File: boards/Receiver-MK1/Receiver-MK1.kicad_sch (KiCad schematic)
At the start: 0 parts

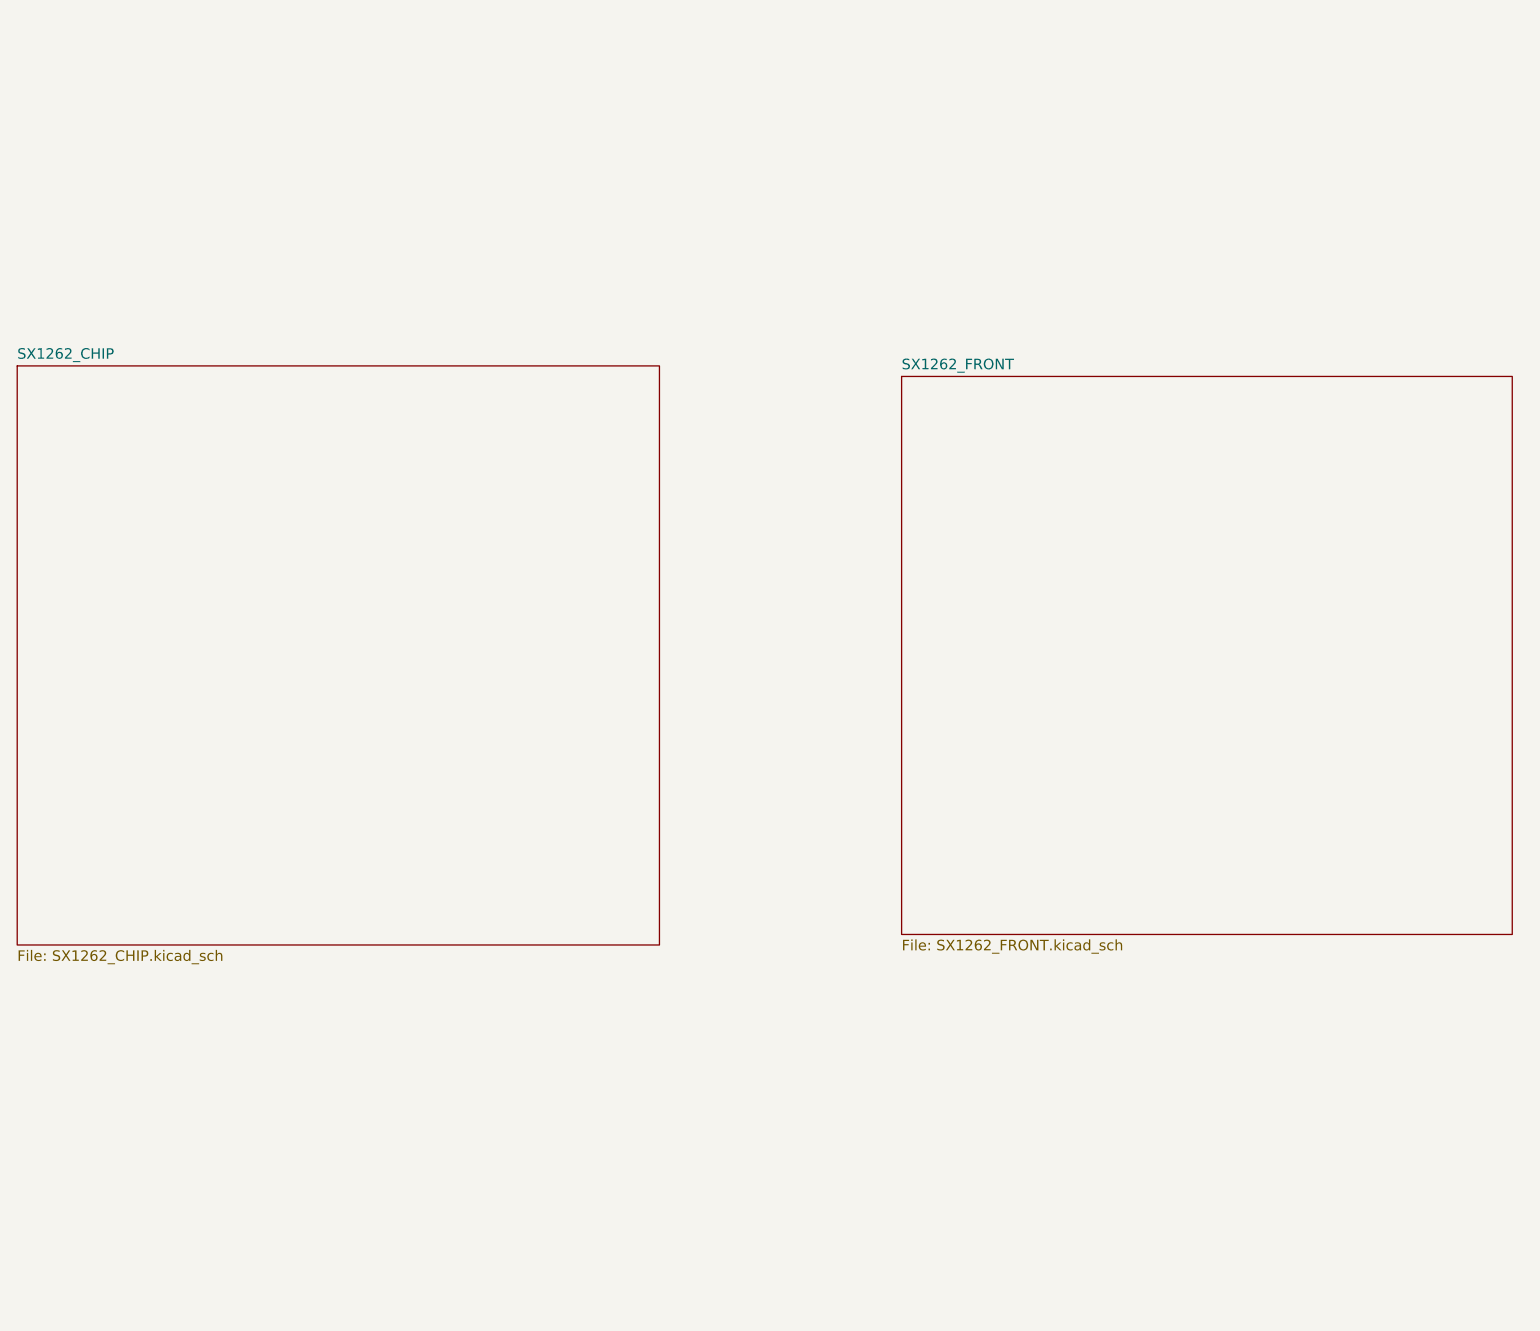
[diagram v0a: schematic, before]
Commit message: Added Transceiver
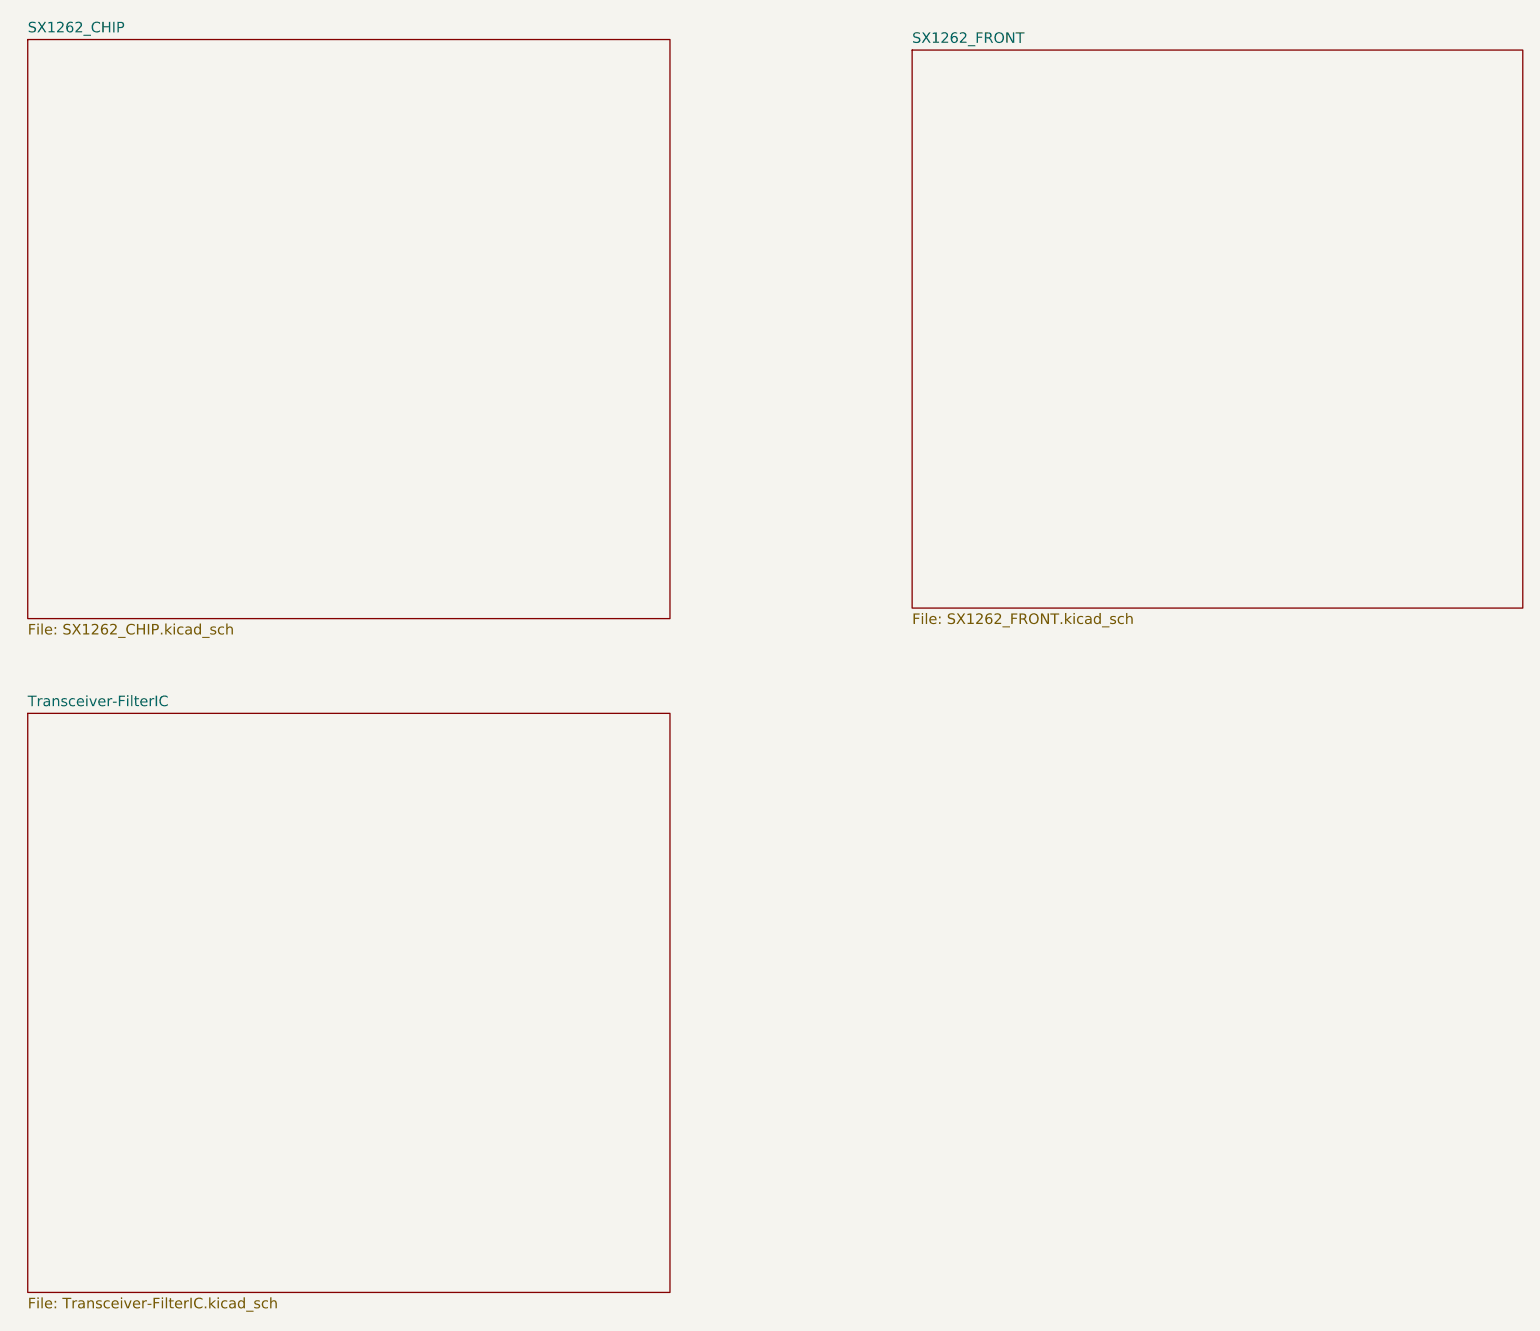
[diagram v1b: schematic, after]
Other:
- added sheet Transceiver-FilterIC (Transceiver-FilterIC.kicad_sch)
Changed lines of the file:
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@@
 	(paper "A4")
 	(sheet
-		(at 55.88 57.15)
+		(at 57.15 17.78)
 		(size 77.47 69.85)
 		(fields_autoplaced yes)
@@
 		)
 		(property "Sheetname" "SX1262_CHIP"
-			(at 55.88 56.4384 0)
+			(at 57.15 17.0684 0)
 			(effects
 				(font
@@
 		)
 		(property "Sheetfile" "SX1262_CHIP.kicad_sch"
-			(at 55.88 127.5846 0)
+			(at 57.15 88.2146 0)
 			(effects
 				(font
@@
 	)
 	(sheet
-		(at 162.56 58.42)
+		(at 163.83 19.05)
 		(size 73.66 67.31)
 		(fields_autoplaced yes)
@@
 		)
 		(property "Sheetname" "SX1262_FRONT"
-			(at 162.56 57.7084 0)
+			(at 163.83 18.3384 0)
 			(effects
 				(font
@@
 		)
 		(property "Sheetfile" "SX1262_FRONT.kicad_sch"
-			(at 162.56 126.3146 0)
+			(at 163.83 86.9446 0)
 			(effects
 				(font
@@
 				)
 			)
+		)
+	)
+	(sheet
+		(at 57.15 99.06)
+		(size 77.47 69.85)
+		(fields_autoplaced yes)
+		(stroke
+			(width 0.1524)
+			(type solid)
+		)
+		(fill
+			(color 0 0 0 0.0000)
+		)
+		(property "Sheetname" "Transceiver-FilterIC"
+			(at 57.15 98.3484 0)
+			(effects
+				(font
+					(size 1.27 1.27)
+				)
+				(justify left bottom)
+			)
+		)
+		(property "Sheetfile" "Transceiver-FilterIC.kicad_sch"
+			(at 57.15 169.4946 0)
+			(effects
+				(font
+					(size 1.27 1.27)
+				)
+				(justify left top)
+			)
+		)
+		(instances
+			(project "Receiver-MK1"
+				(path "/4a9cc9ec-e428-44b1-9ebf-81bf66d6efd4"
+					(page "4")
+				)
+			)
